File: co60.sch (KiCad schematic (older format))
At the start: 20 parts, among them Q1 PZT2222A, SW1 SW_Push, U1 ATMEGA32U4, X1 ASX3F

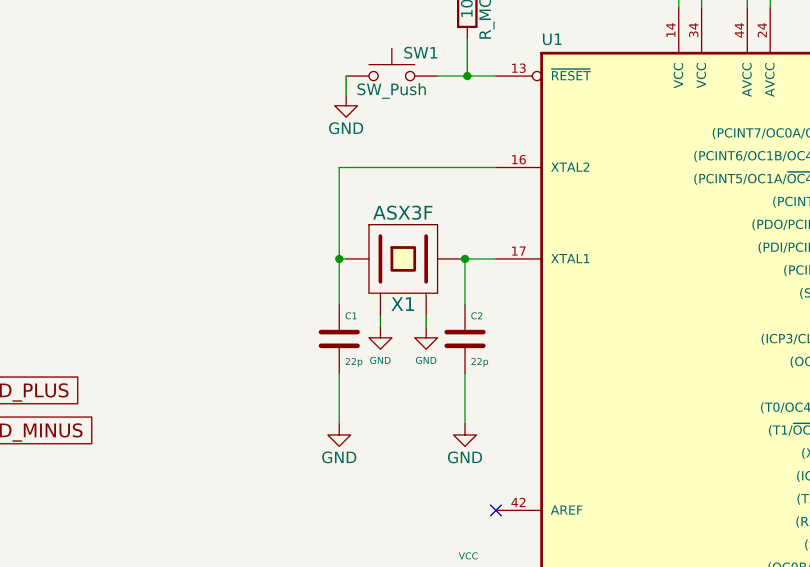
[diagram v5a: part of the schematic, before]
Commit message: Update: Finish assigning footprints, and switch crystals
I had been using the crystal that the GH60 uses, but it looked
like it might be hard to source. Also, some of the bottom row
footprints might need to be reversed, depending on the overlap
of the switches.
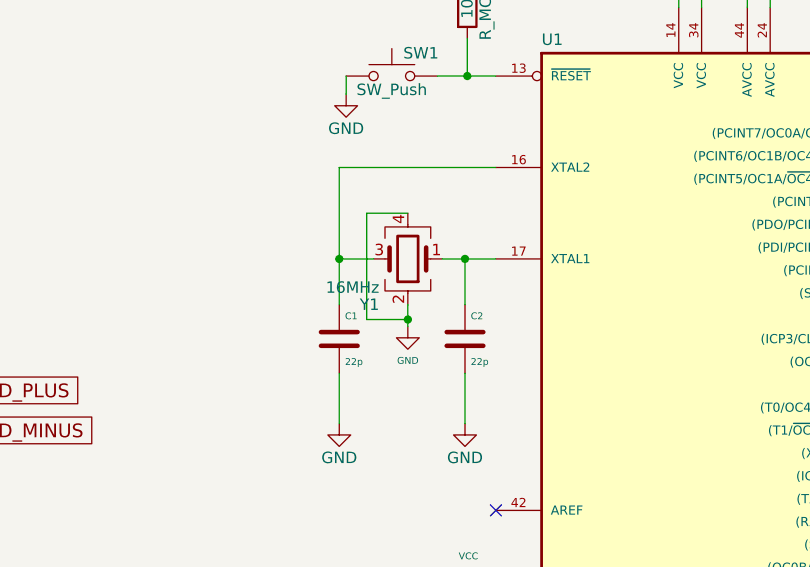
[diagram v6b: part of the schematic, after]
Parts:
- removed X1: ASX3F, ndk:4-SMD, symbol ASX4
- added Y1: 16MHz, Crystals:Crystal_SMD_2520-4pin_2.5x2.0mm, symbol Crystal_GND24
- SW1: footprint (none) -> Buttons_Switches_SMD:SW_SPST_TL3342
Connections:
- net GND: now also Y1.2, Y1.4
- net at C1.1, U1.16 (XTAL2): now also Y1.3
- net at C2.1, U1.17 (XTAL1): now also Y1.1
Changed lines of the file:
@@
-$EndComp
-$Comp
-L ASX4 X1
-U 1 1 5AAB4912
-P 6735 3030
-F 0 "X1" H 6735 2830 60  0000 C CNN
-F 1 "ASX3F" H 6735 3230 60  0000 C CNN
-F 2 "ndk:4-SMD" H 6735 3030 60  0001 C CNN
-F 3 "http://www.ansenquartz.com/Upload/Products/Pro-20151234634734.pdf" H 6735 3030 60  0001 C CNN
-	1    6735 3030
-	1    0    0    -1
 $EndComp
 $Comp
@@
 $Comp
 L GND #PWR06
-U 1 1 5B375157
-P 6635 3325
-F 0 "#PWR06" H 6635 3075 50  0001 C CNN
-F 1 "GND" H 6635 3175 30  0000 C CNN
-F 2 "" H 6635 3325 50  0001 C CNN
-F 3 "" H 6635 3325 50  0001 C CNN
-	1    6635 3325
-	1    0    0    -1
-$EndComp
-$Comp
-L GND #PWR07
 U 1 1 5B375186
-P 6835 3325
-F 0 "#PWR07" H 6835 3075 50  0001 C CNN
-F 1 "GND" H 6835 3175 30  0000 C CNN
-F 2 "" H 6835 3325 50  0001 C CNN
-F 3 "" H 6835 3325 50  0001 C CNN
-	1    6835 3325
+P 6755 3325
+F 0 "#PWR06" H 6755 3075 50  0001 C CNN
+F 1 "GND" H 6755 3175 30  0000 C CNN
+F 2 "" H 6755 3325 50  0001 C CNN
+F 3 "" H 6755 3325 50  0001 C CNN
+	1    6755 3325
 	1    0    0    -1
 $EndComp
@@
 $EndComp
 $Comp
-L GND #PWR08
+L GND #PWR07
 U 1 1 5ABE07D4
 P 3055 5450
-F 0 "#PWR08" H 3055 5200 50  0001 C CNN
+F 0 "#PWR07" H 3055 5200 50  0001 C CNN
 F 1 "GND" H 3055 5300 50  0000 C CNN
 F 2 "" H 3055 5450 50  0001 C CNN
@@
 NoConn ~ 2850 4450
 $Comp
-L VCC #PWR09
+L VCC #PWR08
 U 1 1 5ABF086B
 P 7015 1650
-F 0 "#PWR09" H 7015 1500 50  0001 C CNN
+F 0 "#PWR08" H 7015 1500 50  0001 C CNN
 F 1 "VCC" H 7015 1800 50  0000 C CNN
 F 2 "" H 7015 1650 50  0001 C CNN
@@
 	3190 2435 3190 4550
 Wire Wire Line
-	6635 3280 6635 3325
-Wire Wire Line
-	6835 3280 6835 3325
-Wire Wire Line
 	2850 3050 3000 3050
 Wire Wire Line
@@
 F 0 "SW1" H 6735 2330 50  0000 L CNN
 F 1 "SW_Push" H 6685 2170 50  0000 C CNN
-F 2 "" H 6685 2430 50  0001 C CNN
+F 2 "Buttons_Switches_SMD:SW_SPST_TL3342" H 6685 2430 50  0001 C CNN
 F 3 "" H 6685 2430 50  0001 C CNN
 	1    6685 2230
@@
 $EndComp
 $Comp
-L GND #PWR010
+L GND #PWR09
 U 1 1 5AC1F377
 P 6485 2310
-F 0 "#PWR010" H 6485 2060 50  0001 C CNN
+F 0 "#PWR09" H 6485 2060 50  0001 C CNN
 F 1 "GND" H 6485 2160 50  0000 C CNN
 F 2 "" H 6485 2310 50  0001 C CNN
@@
 LEDGND
 $Comp
-L GND #PWR011
+L GND #PWR010
 U 1 1 5AC27CFC
 P 4995 1475
-F 0 "#PWR011" H 4995 1225 50  0001 C CNN
+F 0 "#PWR010" H 4995 1225 50  0001 C CNN
 F 1 "GND" H 4995 1325 50  0000 C CNN
 F 2 "" H 4995 1475 50  0001 C CNN
@@
 	4465 1080 4695 1080
 $Comp
-L PWR_FLAG #FLG012
+L PWR_FLAG #FLG011
 U 1 1 5AC2942E
 P 3400 2605
-F 0 "#FLG012" H 3400 2680 50  0001 C CNN
+F 0 "#FLG011" H 3400 2680 50  0001 C CNN
 F 1 "PWR_FLAG" H 3400 2755 50  0000 C CNN
 F 2 "" H 3400 2605 50  0001 C CNN
@@
 Connection ~ 3190 2605
 $Comp
-L PWR_FLAG #FLG013
+L PWR_FLAG #FLG012
 U 1 1 5AC2A5F1
 P 3360 5460
-F 0 "#FLG013" H 3360 5535 50  0001 C CNN
+F 0 "#FLG012" H 3360 5535 50  0001 C CNN
 F 1 "PWR_FLAG" H 3360 5610 50  0000 C CNN
 F 2 "" H 3360 5460 50  0001 C CNN
@@
 	9765 4580 9765 4755
 $Comp
-L GND #PWR014
+L GND #PWR013
 U 1 1 5AC734D3
 P 9765 5185
-F 0 "#PWR014" H 9765 4935 50  0001 C CNN
+F 0 "#PWR013" H 9765 4935 50  0001 C CNN
 F 1 "GND" H 9765 5035 50  0000 C CNN
 F 2 "" H 9765 5185 50  0001 C CNN
@@
 NoConn ~ 9140 5180
 $Comp
-L GND #PWR015
+L GND #PWR014
 U 1 1 5AC75DE6
 P 8290 6040
-F 0 "#PWR015" H 8290 5790 50  0001 C CNN
+F 0 "#PWR014" H 8290 5790 50  0001 C CNN
 F 1 "GND" H 8290 5890 30  0000 C CNN
 F 2 "" H 8290 6040 50  0001 C CNN
@@
 $EndComp
 $Comp
-L GND #PWR016
+L GND #PWR015
 U 1 1 5AC7689B
 P 8190 6040
-F 0 "#PWR016" H 8190 5790 50  0001 C CNN
+F 0 "#PWR015" H 8190 5790 50  0001 C CNN
 F 1 "GND" H 8190 5890 30  0000 C CNN
 F 2 "" H 8190 6040 50  0001 C CNN
@@
 $EndComp
 $Comp
-L GND #PWR017
+L GND #PWR016
 U 1 1 5AC768E5
 P 8090 6040
-F 0 "#PWR017" H 8090 5790 50  0001 C CNN
+F 0 "#PWR016" H 8090 5790 50  0001 C CNN
 F 1 "GND" H 8090 5890 30  0000 C CNN
 F 2 "" H 8090 6040 50  0001 C CNN
@@
 $EndComp
 $Comp
-L GND #PWR018
+L GND #PWR017
 U 1 1 5AC7692F
 P 7990 6040
-F 0 "#PWR018" H 7990 5790 50  0001 C CNN
+F 0 "#PWR017" H 7990 5790 50  0001 C CNN
 F 1 "GND" H 7990 5890 30  0000 C CNN
 F 2 "" H 7990 6040 50  0001 C CNN
@@
 	8290 5930 8290 6040
 $Comp
-L GND #PWR019
+L GND #PWR018
 U 1 1 5AC78483
 P 6975 6040
-F 0 "#PWR019" H 6975 5790 50  0001 C CNN
+F 0 "#PWR018" H 6975 5790 50  0001 C CNN
 F 1 "GND" H 6975 5890 30  0000 C CNN
 F 2 "" H 6975 6040 50  0001 C CNN
@@
 	6675 5180 6675 5555
 $Comp
-L GND #PWR020
+L GND #PWR019
 U 1 1 5AC79A5C
 P 6675 6040
-F 0 "#PWR020" H 6675 5790 50  0001 C CNN
+F 0 "#PWR019" H 6675 5790 50  0001 C CNN
 F 1 "GND" H 6675 5890 30  0000 C CNN
 F 2 "" H 6675 6040 50  0001 C CNN
@@
 NoConn ~ 7140 4130
 $Comp
-L VCC #PWR021
+L VCC #PWR020
 U 1 1 5AC7DE21
 P 8340 1815
-F 0 "#PWR021" H 8340 1665 50  0001 C CNN
+F 0 "#PWR020" H 8340 1665 50  0001 C CNN
 F 1 "VCC" H 8340 1965 30  0000 C CNN
 F 2 "" H 8340 1815 50  0001 C CNN
@@
 $EndComp
 $Comp
-L VCC #PWR022
+L VCC #PWR021
 U 1 1 5AC7F341
 P 8240 1815
-F 0 "#PWR022" H 8240 1665 50  0001 C CNN
+F 0 "#PWR021" H 8240 1665 50  0001 C CNN
 F 1 "VCC" H 8240 1965 30  0000 C CNN
 F 2 "" H 8240 1815 50  0001 C CNN
@@
 $EndComp
 $Comp
-L VCC #PWR023
+L VCC #PWR022
 U 1 1 5AC7F38B
 P 8040 1815
-F 0 "#PWR023" H 8040 1665 50  0001 C CNN
+F 0 "#PWR022" H 8040 1665 50  0001 C CNN
 F 1 "VCC" H 8040 1965 30  0000 C CNN
 F 2 "" H 8040 1815 50  0001 C CNN
@@
 $EndComp
 $Comp
-L VCC #PWR024
+L VCC #PWR023
 U 1 1 5AC7F3D5
 P 7940 1815
-F 0 "#PWR024" H 7940 1665 50  0001 C CNN
+F 0 "#PWR023" H 7940 1665 50  0001 C CNN
 F 1 "VCC" H 7940 1965 30  0000 C CNN
 F 2 "" H 7940 1815 50  0001 C CNN
@@
 	7940 1815 7940 1930
 $Comp
-L VCC #PWR025
+L VCC #PWR024
 U 1 1 5AC80BD7
 P 7020 4480
-F 0 "#PWR025" H 7020 4330 50  0001 C CNN
+F 0 "#PWR024" H 7020 4330 50  0001 C CNN
 F 1 "VCC" H 7020 4630 30  0000 C CNN
 F 2 "" H 7020 4480 50  0001 C CNN
@@
 	6455 3530 6455 3750
 Wire Wire Line
-	6485 3030 6455 3030
-Wire Wire Line
 	6455 2630 6455 3230
-Wire Wire Line
-	6985 3030 7140 3030
-Wire Wire Line
-	7005 3030 7005 3230
-Connection ~ 7005 3030
 Wire Wire Line
 	6455 2630 7140 2630
@@
 Wire Wire Line
 	9140 5380 9295 5380
+$Comp
+L Crystal_GND24 Y1
+U 1 1 5ADF9892
+P 6755 3030
+F 0 "Y1" H 6880 3230 50  0000 L CNN
+F 1 "16MHz" H 6880 3155 50  0000 L CNN
+F 2 "Crystals:Crystal_SMD_2520-4pin_2.5x2.0mm" H 6755 3030 50  0001 C CNN
+F 3 "http://www.newxtal.com/UploadFiles/Images/2012-11-12-09-29-09-776.pdf" H 6755 3030 50  0001 C CNN
+	1    6755 3030
+	-1   0    0    1
+$EndComp
+Wire Wire Line
+	7140 3030 6905 3030
+Wire Wire Line
+	6605 3030 6455 3030
+Wire Wire Line
+	6755 3230 6755 3325
+Wire Wire Line
+	6755 2830 6575 2830
+Wire Wire Line
+	6575 2830 6575 3295
+Wire Wire Line
+	6575 3295 6755 3295
+Connection ~ 6755 3295
+Wire Wire Line
+	7005 3230 7005 3030
+Connection ~ 7005 3030
 $EndSCHEMATC

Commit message: Update: Add ESD protection, work on bottom row layout
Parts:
- added DP1: PRTR5V0U2X, locallib:SOT143B, symbol PRTR5V0U2X
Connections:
- net GND: now also DP1.1 (GND)
- net VCC: now also DP1.4 (VCC)
- net at R_USB_1.2, USB1.18 (Dp2), USB1.6 (Dp1): now also DP1.2 (IO1)
- net at R_USB_2.2, USB1.19 (Dn2), USB1.7 (Dn1): now also DP1.3 (IO2)
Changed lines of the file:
@@
 LIBS:contrib
 LIBS:valves
+LIBS:aker
+LIBS:atmega32u4
+LIBS:ESD_Protection
 LIBS:MX_Alps_Hybrids
-LIBS:aker
 LIBS:Type-C
-LIBS:atmega32u4
 LIBS:co60-cache
 EELAYER 25 0
@@
 	7005 3230 7005 3030
 Connection ~ 7005 3030
+$Comp
+L PRTR5V0U2X DP1
+U 1 1 5ADFD2C3
+P 4285 4320
+F 0 "DP1" H 4285 4570 50  0000 C CNN
+F 1 "PRTR5V0U2X" H 4285 4070 50  0000 C CNN
+F 2 "locallib:SOT143B" H 4335 4270 50  0001 C CNN
+F 3 "https://assets.nexperia.com/documents/data-sheet/PRTR5V0U2X.pdf" H 4335 4270 50  0001 C CNN
+	1    4285 4320
+	1    0    0    -1
+$EndComp
+$Comp
+L GND #PWR025
+U 1 1 5ADFD846
+P 3855 4630
+F 0 "#PWR025" H 3855 4380 50  0001 C CNN
+F 1 "GND" H 3855 4480 50  0000 C CNN
+F 2 "" H 3855 4630 50  0001 C CNN
+F 3 "" H 3855 4630 50  0001 C CNN
+	1    3855 4630
+	1    0    0    -1
+$EndComp
+Wire Wire Line
+	3985 4420 3855 4420
+Wire Wire Line
+	3855 4420 3855 4630
+$Comp
+L VCC #PWR026
+U 1 1 5ADFDCBF
+P 3850 4125
+F 0 "#PWR026" H 3850 3975 50  0001 C CNN
+F 1 "VCC" H 3850 4275 50  0000 C CNN
+F 2 "" H 3850 4125 50  0001 C CNN
+F 3 "" H 3850 4125 50  0001 C CNN
+	1    3850 4125
+	1    0    0    -1
+$EndComp
+Wire Wire Line
+	3985 4220 3850 4220
+Wire Wire Line
+	3850 4220 3850 4125
+Wire Wire Line
+	4585 4220 4585 4015
+Wire Wire Line
+	4585 4015 3930 4015
+Wire Wire Line
+	3930 4015 3930 3605
+Connection ~ 3930 3605
+Wire Wire Line
+	4585 4420 4630 4420
+Wire Wire Line
+	4630 4420 4630 3950
+Wire Wire Line
+	4630 3950 4060 3950
+Wire Wire Line
+	4060 3950 4060 3780
+Connection ~ 4060 3780
 $EndSCHEMATC

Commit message: Add: Begin working on PCB layout
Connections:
- net GND: now also USB1.26 (Connector_Legs), USB1.27 (Under-Barrel_Pads)
- no-connect marks 17 -> 15
